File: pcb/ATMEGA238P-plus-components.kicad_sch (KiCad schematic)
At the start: 70 parts, among them J15 ICSP, J16 USB_B_Micro, J17 Conn_Coaxial, SW3 TS24CA_C393942, U3 ATMEGA328P-AU, U4 CH340G, U5 LM358DR, U6 74HC245, U7 nRF24L01P, U8 MICROSD_C164170, U9 74AHC1G125, Y3 16MHz, Y4 12MHz, Y5 16MHz

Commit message: pcb: switch SW1-SW3 to the TC-6610 THT tact switch (C7528713)
Replace the low-profile side-actuated TS24CA with a tall 9mm 6x6 THT
button that stays reachable on the assembled frame. The 4-pin part has
internally shorted pin pairs across its 6.5mm axis, so the distinct
1/2/3/4 pad numbering of the converted EasyEDA footprint would strap
each net across a shorted pair (STM32 held in reset); use KiCad's
official SW_PUSH_6mm_H9.5mm instead, whose paired 1,1,2,2 pads encode
the topology and drop onto the existing 2-pin symbols. Headless KiCad
10 ERC is identical before and after.
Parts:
- SW3: value TS24CA_C393942 -> TC-6610_C7528713; footprint easyeda:SW-SMD_2P-TS24CA -> Button_Switch_THT:SW_PUSH_6mm_H9.5mm; LCSC C393942 -> C7528713; Manufacturer SHOU HAN -> FG; Part TS24CA -> TC-6610 -6*6*9-260g
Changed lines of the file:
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@@
 			)
 		)
-		(property "Value" "TS24CA_C393942"
+		(property "Value" "TC-6610_C7528713"
 			(at 33.02 40.6399 90)
 			(hide yes)
@@
 			)
 		)
-		(property "Footprint" "easyeda:SW-SMD_2P-TS24CA"
+		(property "Footprint" "Button_Switch_THT:SW_PUSH_6mm_H9.5mm"
 			(at 34.29 39.37 0)
 			(hide yes)
@@
 			)
 		)
-		(property "Datasheet" "https://www.lcsc.com/datasheet/lcsc_datasheet_2404241539_SHOU-HAN-TS24CA_C393942.pdf"
+		(property "Datasheet" "https://wmsc.lcsc.com/wmsc/upload/file/pdf/v2/lcsc/2401191746_FG-TC-6610--6-6-9-260g_C7528713.pdf"
 			(at 34.29 39.37 0)
 			(hide yes)
@@
 			)
 		)
-		(property "Description" "Push button switch, generic, two pins"
+		(property "Description" "-20℃~+70℃ 12V 2.6N 50,000 cycles 50mA 6mm 6mm Black Round Button SPST Through Hole Without Bracket 插件-4P,6x6mm Tactile Switches ROHS"
 			(at 29.21 39.37 0)
 			(hide yes)
@@
 			)
 		)
-		(property "LCSC" "C393942"
+		(property "LCSC" "C7528713"
 			(at 29.21 39.37 0)
 			(hide yes)
@@
 			)
 		)
-		(property "Part" "TS24CA"
+		(property "Part" "TC-6610 -6*6*9-260g"
 			(at 29.21 39.37 0)
 			(hide yes)
@@
 			)
 		)
-		(property "Manufacturer" "SHOU HAN"
+		(property "Manufacturer" "FG"
 			(at 29.21 39.37 0)
 			(hide yes)

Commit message: pcb: 3D models for U3, U5, J3, J16
U3 and U5 move from the model-less DigiKey footprints to the official
KiCad TQFP-32 and SOIC-8 footprints, whose STEP models ship with the
AppImage. J3/J16's micro-USB footprint had no model, no MPN, and
unknown provenance - replaced wholesale with the SHOU HAN MicroXNJ
(C404969): converted footprint with shell legs renumbered to the
Shield pin 6, STEP model, and BOM fields, verified against its
datasheet drawing. ERC caught that the LM358 is multi-unit and the
first edit only touched U5A's footprint field; U5B fixed to match.
Headless KiCad 10 ERC identical to baseline.
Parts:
- J16: footprint easyeda:MICRO-USB-SMD_5P-P0.65-H-F_MICRO5.9MMUSB -> easyeda:MICRO-USB-SMD_MICROXNJ_1; LCSC (none) -> C404969; Manufacturer (none) -> SHOU HAN; Part (none) -> MicroXNJ
- U3: footprint digikey-footprints:TQFP-32_7x7mm -> Package_QFP:TQFP-32_7x7mm_P0.8mm
- U5: footprint digikey-footprints:SOIC-8_W3.9mm -> Package_SO:SOIC-8_3.9x4.9mm_P1.27mm
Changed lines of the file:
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@@
 			)
 		)
-		(property "Footprint" "digikey-footprints:SOIC-8_W3.9mm"
+		(property "Footprint" "Package_SO:SOIC-8_3.9x4.9mm_P1.27mm"
 			(at 41.91 203.2 0)
 			(hide yes)
@@
 			)
 		)
-		(property "Footprint" "easyeda:MICRO-USB-SMD_5P-P0.65-H-F_MICRO5.9MMUSB"
+		(property "Footprint" "easyeda:MICRO-USB-SMD_MICROXNJ_1"
 			(at 43.18 247.65 0)
 			(hide yes)
@@
 			)
 		)
-		(property "Datasheet" ""
+		(property "Datasheet" "https://www.lcsc.com/datasheet/lcsc_datasheet_2204151400_SHOU-HAN-MicroXNJ_C404969.pdf"
 			(at 43.18 247.65 0)
 			(hide yes)
@@
 			)
 		)
-		(property "Description" "USB Micro Type B connector"
+		(property "Description" "-20℃~+85℃ 1 1.8A 30V 5,000 times 5P Black Female Micro-B Surface Mount, Right Angle USB 2.0 SMD USB Connectors ROHS"
 			(at 39.37 246.38 0)
 			(hide yes)
@@
 			)
 		)
+    (property "LCSC" "C404969" (at 39.37 246.38 0)
+      (effects (font (size 1.27 1.27)) (hide yes))
+    )
+    (property "Part" "MicroXNJ" (at 39.37 246.38 0)
+      (effects (font (size 1.27 1.27)) (hide yes))
+    )
+    (property "Manufacturer" "SHOU HAN" (at 39.37 246.38 0)
+      (effects (font (size 1.27 1.27)) (hide yes))
+    )
 		(pin "3"
 		)
@@
 			)
 		)
-		(property "Footprint" "digikey-footprints:TQFP-32_7x7mm"
+		(property "Footprint" "Package_QFP:TQFP-32_7x7mm_P0.8mm"
 			(at 171.45 87.63 0)
 			(hide yes)
@@
 			)
 		)
-		(property "Footprint" "digikey-footprints:SOIC-8_W3.9mm"
+		(property "Footprint" "Package_SO:SOIC-8_3.9x4.9mm_P1.27mm"
 			(at 41.91 180.34 0)
 			(hide yes)

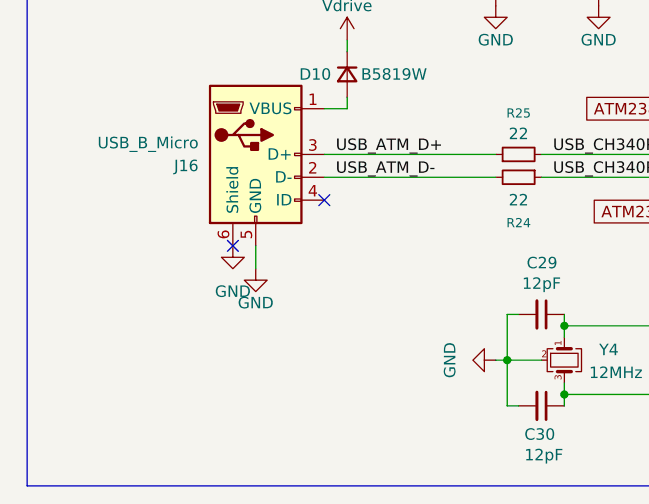
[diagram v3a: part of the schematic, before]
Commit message: pcb: import the new U3/U5/USB footprints onto the board
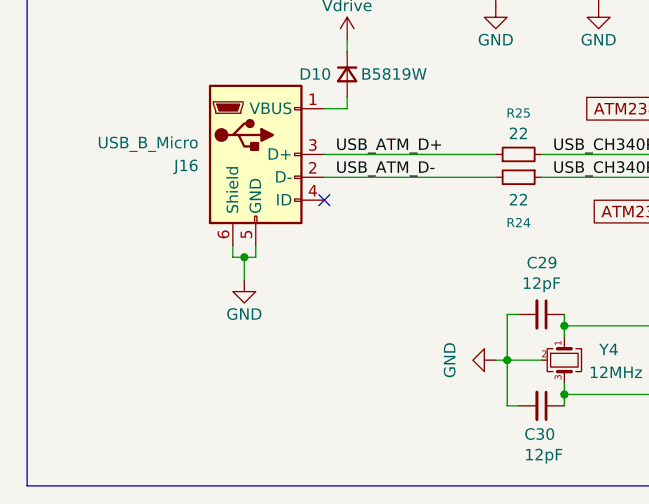
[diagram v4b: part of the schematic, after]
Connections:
- no-connect marks 20 -> 19
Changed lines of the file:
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@@
 	)
 	(junction
+		(at 38.1 257.81)
+		(diameter 0)
+		(color 0 0 0 0)
+	)
+	(junction
 		(at 177.8 256.54)
 		(diameter 0)
@@
 	)
 	(no_connect
-		(at 36.83 256.54)
-	)
-	(no_connect
 		(at 153.67 80.01)
 	)
@@
 	(wire
 		(pts
-			(xy 39.37 256.54) (xy 39.37 259.08)
+			(xy 38.1 257.81) (xy 38.1 260.35)
 		)
 		(stroke
@@
 	(wire
 		(pts
+			(xy 39.37 257.81) (xy 39.37 256.54)
+		)
+		(stroke
+			(width 0)
+			(type default)
+		)
+	)
+	(wire
+		(pts
 			(xy 118.11 238.76) (xy 115.57 238.76)
 		)
@@
 	(wire
 		(pts
+			(xy 38.1 257.81) (xy 39.37 257.81)
+		)
+		(stroke
+			(width 0)
+			(type default)
+		)
+	)
+	(wire
+		(pts
 			(xy 91.44 254) (xy 91.44 265.43)
 		)
@@
 	(wire
 		(pts
+			(xy 36.83 257.81) (xy 38.1 257.81)
+		)
+		(stroke
+			(width 0)
+			(type default)
+		)
+	)
+	(wire
+		(pts
 			(xy 274.32 241.3) (xy 274.32 243.84)
 		)
@@
 	(wire
 		(pts
+			(xy 36.83 256.54) (xy 36.83 257.81)
+		)
+		(stroke
+			(width 0)
+			(type default)
+		)
+	)
+	(wire
+		(pts
 			(xy 173.99 27.94) (xy 173.99 22.86)
 		)
@@
 	(symbol
 		(lib_id "PCM_SparkFun-PowerSymbol:GND")
-		(at 39.37 259.08 0)
+		(at 38.1 260.35 0)
 		(unit 1)
 		(body_style 1)
@@
 		(fields_autoplaced yes)
 		(property "Reference" "#PWR079"
-			(at 39.37 265.43 0)
+			(at 38.1 266.7 0)
 			(hide yes)
 			(show_name no)
@@
 		)
 		(property "Value" "GND"
-			(at 39.37 262.89 0)
+			(at 38.1 264.16 0)
 			(show_name no)
 			(do_not_autoplace yes)
@@
 		)
 		(property "Footprint" ""
-			(at 39.37 259.08 0)
+			(at 38.1 260.35 0)
 			(hide yes)
 			(show_name no)
@@
 		)
 		(property "Datasheet" ""
-			(at 39.37 259.08 0)
+			(at 38.1 260.35 0)
 			(hide yes)
 			(show_name no)
@@
 		)
 		(property "Description" "Power symbol creates a global label with name \"GND\" , ground"
-			(at 39.37 267.97 0)
+			(at 38.1 269.24 0)
 			(hide yes)
 			(show_name no)
@@
 			)
 		)
-    (property "LCSC" "C404969" (at 39.37 246.38 0)
-      (effects (font (size 1.27 1.27)) (hide yes))
-    )
-    (property "Part" "MicroXNJ" (at 39.37 246.38 0)
-      (effects (font (size 1.27 1.27)) (hide yes))
-    )
-    (property "Manufacturer" "SHOU HAN" (at 39.37 246.38 0)
-      (effects (font (size 1.27 1.27)) (hide yes))
-    )
+		(property "LCSC" "C404969"
+			(at 39.37 246.38 0)
+			(hide yes)
+			(show_name no)
+			(do_not_autoplace no)
+			(effects
+				(font
+					(size 1.27 1.27)
+				)
+			)
+		)
+		(property "Part" "MicroXNJ"
+			(at 39.37 246.38 0)
+			(hide yes)
+			(show_name no)
+			(do_not_autoplace no)
+			(effects
+				(font
+					(size 1.27 1.27)
+				)
+			)
+		)
+		(property "Manufacturer" "SHOU HAN"
+			(at 39.37 246.38 0)
+			(hide yes)
+			(show_name no)
+			(do_not_autoplace no)
+			(effects
+				(font
+					(size 1.27 1.27)
+				)
+			)
+		)
 		(pin "3"
 		)
@@
 					(unit 1)
 				)
-			)
-		)
-	)
-	(symbol
-		(lib_id "power:GND")
-		(at 36.83 256.54 0)
-		(unit 1)
-		(body_style 1)
-		(exclude_from_sim no)
-		(in_bom yes)
-		(on_board yes)
-		(in_pos_files yes)
-		(dnp no)
-		(fields_autoplaced yes)
-		(property "Reference" "#PWR0143"
-			(at 36.83 262.89 0)
-			(hide yes)
-			(show_name no)
-			(do_not_autoplace no)
-			(effects
-				(font
-					(size 1.27 1.27)
-				)
-			)
-		)
-		(property "Value" "GND"
-			(at 36.83 261.62 0)
-			(show_name no)
-			(do_not_autoplace no)
-			(effects
-				(font
-					(size 1.27 1.27)
-				)
-			)
-		)
-		(property "Footprint" ""
-			(at 36.83 256.54 0)
-			(hide yes)
-			(show_name no)
-			(do_not_autoplace no)
-			(effects
-				(font
-					(size 1.27 1.27)
-				)
-			)
-		)
-		(property "Datasheet" ""
-			(at 36.83 256.54 0)
-			(hide yes)
-			(show_name no)
-			(do_not_autoplace no)
-			(effects
-				(font
-					(size 1.27 1.27)
-				)
-			)
-		)
-		(property "Description" "Power symbol creates a global label with name GND, ground"
-			(at 36.83 256.54 0)
-			(hide yes)
-			(show_name no)
-			(do_not_autoplace no)
-			(effects
-				(font
-					(size 1.27 1.27)
-				)
-			)
-		)
-		(pin "1"
-		)
-		(instances
-			(project "drone-flight-controller"
-				(path "/2753c1d5-c5b3-42f6-8923-cca974813b6b/3ba11137-7aba-429f-b0d2-26d56a1546d6"
-					(reference "#PWR0143")
-					(unit 1)
-				)

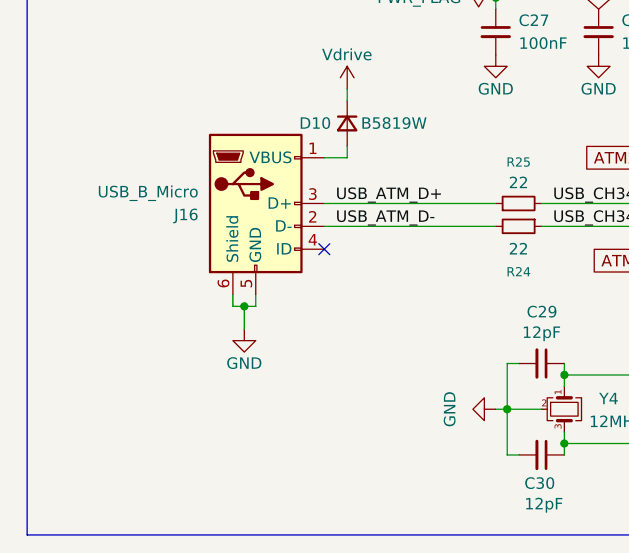
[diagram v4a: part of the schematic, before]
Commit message: pcb: session state - U10 folded on board, pending sch fixes
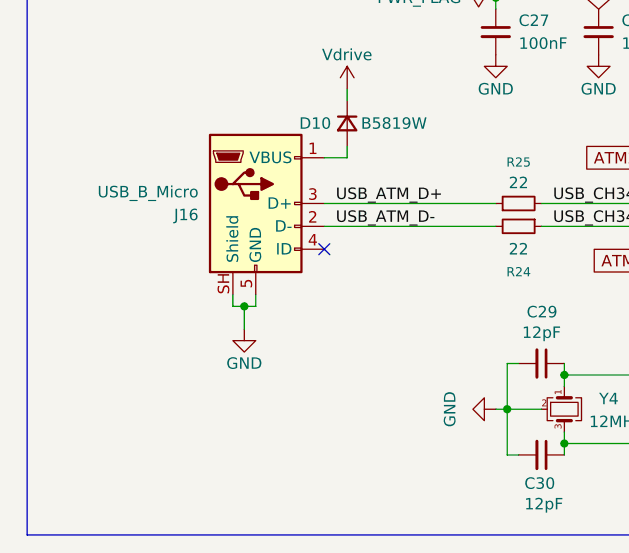
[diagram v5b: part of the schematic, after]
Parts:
- U3: footprint Package_QFP:TQFP-32_7x7mm_P0.8mm -> digikey-footprints:TQFP-32_7x7mm
- U5: footprint Package_SO:SOIC-8_3.9x4.9mm_P1.27mm -> digikey-footprints:SOIC-8_W3.9mm
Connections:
- net GND: now also J16.SH (Shield); no longer J16.6 (Shield)
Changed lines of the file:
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@@
 			)
 		)
-		(property "Footprint" "Package_SO:SOIC-8_3.9x4.9mm_P1.27mm"
+		(property "Footprint" "digikey-footprints:SOIC-8_W3.9mm"
 			(at 41.91 203.2 0)
 			(hide yes)
@@
 			)
 		)
-		(property "Description" "-20℃~+85℃ 1 1.8A 30V 5,000 times 5P Black Female Micro-B Surface Mount, Right Angle USB 2.0 SMD USB Connectors ROHS"
+		(property "Description" "USB Micro Type B connector"
 			(at 39.37 246.38 0)
 			(hide yes)
@@
 		(pin "1"
 		)
-		(pin "6"
+		(pin "SH"
 		)
 		(pin "4"
@@
 			)
 		)
-		(property "Description" "-20℃~+70℃ 12V 2.6N 50,000 cycles 50mA 6mm 6mm Black Round Button SPST Through Hole Without Bracket 插件-4P,6x6mm Tactile Switches ROHS"
+		(property "Description" "Push button switch, generic, two pins"
 			(at 29.21 39.37 0)
 			(hide yes)
@@
 			)
 		)
-		(property "Footprint" "Package_QFP:TQFP-32_7x7mm_P0.8mm"
+		(property "Footprint" "digikey-footprints:TQFP-32_7x7mm"
 			(at 171.45 87.63 0)
 			(hide yes)
@@
 			)
 		)
-		(property "Footprint" "Package_SO:SOIC-8_3.9x4.9mm_P1.27mm"
+		(property "Footprint" "digikey-footprints:SOIC-8_W3.9mm"
 			(at 41.91 180.34 0)
 			(hide yes)

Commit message: pcb: re-apply U3/U5 footprints durably; fix U10 sch/board mismatch and U2 3D path
A symbol-update-with-reset-fields pass reverted U3 and U5 to the
model-less DigiKey footprints because the embedded library defaults
still carried them - re-apply the official footprints on the instances
AND the embedded lib_symbol defaults so a future reset cannot regress
them again. Align U10's schematic with the board's folded
TO-220-3_Horizontal_TabDown (the schematic still said the 4-lead
variant, which a footprint-replacing import would have restored). Point
U2's model at the QFN-24 EP2.6x2.6 step that actually ships - the
Sensor_Motion footprint references an EP2.7x2.6 file that does not
exist in the 3D lib. ERC otherwise identical; two new intentional
lib_symbol_mismatch warnings record that the embedded ATmega/LM7805
defaults now deliberately diverge from the external libraries.
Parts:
- U3: footprint digikey-footprints:TQFP-32_7x7mm -> Package_QFP:TQFP-32_7x7mm_P0.8mm
- U5: footprint digikey-footprints:SOIC-8_W3.9mm -> Package_SO:SOIC-8_3.9x4.9mm_P1.27mm
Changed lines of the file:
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@@
 			)
 		)
-		(property "Footprint" "digikey-footprints:SOIC-8_W3.9mm"
+		(property "Footprint" "Package_SO:SOIC-8_3.9x4.9mm_P1.27mm"
 			(at 41.91 203.2 0)
 			(hide yes)
@@
 			)
 		)
-		(property "Footprint" "digikey-footprints:TQFP-32_7x7mm"
+		(property "Footprint" "Package_QFP:TQFP-32_7x7mm_P0.8mm"
 			(at 171.45 87.63 0)
 			(hide yes)
@@
 			)
 		)
-		(property "Footprint" "digikey-footprints:SOIC-8_W3.9mm"
+		(property "Footprint" "Package_SO:SOIC-8_3.9x4.9mm_P1.27mm"
 			(at 41.91 180.34 0)
 			(hide yes)

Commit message: pcb: source the entire remaining BOM against the LCSC catalog
Jellybean MPN sweep: ~142 refs across 61 groups - every IC, passive,
LED, diode, crystal, RF inductor, ferrite, and connector now carries
LCSC/Part/Manufacturer/Datasheet fields, resolved offline Basic-first.
Crystals were matched on load capacitance to the repo's original
datasheets, the polarized 10uF pair is the exact original tantalum,
and the nRF matching network gets proper RF multilayer parts. Two
physical deltas: Y2's footprint grows 2012 -> 3215 to fit the Basic
Epson FC-135, and FB1/FB2's invalid "100Uhm" value becomes the
sourced 3A 120R power bead. Sourcing gate: PASS, 0 blocking, 26
Extended lines (~$78 max setup). ERC identical.
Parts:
- C20, C21, C22, C24, C27, C28, C31, C32, C33, C45, C47: LCSC (none) -> C1525; Manufacturer (none) -> Samsung Electro-Mechanics; Part (none) -> CL05B104KO5NNNC
- C23, C46: LCSC (none) -> C307423; Manufacturer (none) -> Samsung Electro-Mechanics; Part (none) -> CL05A475MQ5NRNC
- C25, C26, C29, C30, C43, C44: LCSC (none) -> C1547; Manufacturer (none) -> FH(Guangdong Fenghua Advanced Tech); Part (none) -> 0402CG120J500NT
- C34, C35, C36: LCSC (none) -> C15195; Manufacturer (none) -> Samsung Electro-Mechanics; Part (none) -> CL05B103KB5NNNC
- C37: LCSC (none) -> C52923; Manufacturer (none) -> Samsung Electro-Mechanics; Part (none) -> CL05A105KA5NQNC
- C38: LCSC (none) -> C106862; Manufacturer (none) -> YAGEO; Part (none) -> CC0402KRX7R9BB333
- C39: LCSC (none) -> C1552; Manufacturer (none) -> FH(Guangdong Fenghua Advanced Tech); Part (none) -> 0402CG1R5C500NT
- C40: LCSC (none) -> C1550; Manufacturer (none) -> FH(Guangdong Fenghua Advanced Tech); Part (none) -> 0402CG1R0C500NT
- C41: LCSC (none) -> C1531; Manufacturer (none) -> FH(Guangdong Fenghua Advanced Tech); Part (none) -> 0402B222K500NT
- C42: LCSC (none) -> C1538; Manufacturer (none) -> FH(Guangdong Fenghua Advanced Tech); Part (none) -> 0402B472K500NT
- D10: LCSC (none) -> C64885; Manufacturer (none) -> MDD（Microdiode Electronics）; Part (none) -> B5819W
- D11, D12, D18: LCSC (none) -> C12624; Manufacturer (none) -> Hubei KENTO Elec; Part (none) -> KT-0603G
- D13, D15: LCSC (none) -> C2286; Manufacturer (none) -> Hubei KENTO Elec; Part (none) -> KT-0603R
- D16: LCSC (none) -> C2288; Manufacturer (none) -> Hubei KENTO Elec; Part (none) -> KT-0603B
- J15: LCSC (none) -> C492420; Manufacturer (none) -> XFCN; Part (none) -> PZ254V-12-6P
- J17: LCSC (none) -> C496551; Manufacturer (none) -> BAT WIRELESS; Part (none) -> BWSMA-KWE-Z001
- L2: LCSC (none) -> C98003; Manufacturer (none) -> Murata Electronics; Part (none) -> LQG15HS8N2J02D
- L3: LCSC (none) -> C14033; Manufacturer (none) -> Sunlord; Part (none) -> SDCL1005C3N9STDF
- L4: LCSC (none) -> C27123; Manufacturer (none) -> Sunlord; Part (none) -> SDCL1005C2N7STDF
- R21, R30, R33, R35, R36: LCSC (none) -> C25744; Manufacturer (none) -> UNI-ROYAL(Uniroyal Elec); Part (none) -> 0402WGF1002TCE
- R22: LCSC (none) -> C25104; Manufacturer (none) -> UNI-ROYAL(Uniroyal Elec); Part (none) -> 0402WGF3300TCE
- R23, R28, R32: LCSC (none) -> C21190; Manufacturer (none) -> UNI-ROYAL(Uniroyal Elec); Part (none) -> 0603WAF1001T5E
- R24, R25: LCSC (none) -> C25092; Manufacturer (none) -> UNI-ROYAL(Uniroyal Elec); Part (none) -> 0402WGF220JTCE
- R26, R27: LCSC (none) -> C11702; Manufacturer (none) -> UNI-ROYAL(Uniroyal Elec); Part (none) -> 0402WGF1001TCE
- R29, R31: LCSC (none) -> C22843; Manufacturer (none) -> UNI-ROYAL(Uniroyal Elec); Part (none) -> 0603WAF1501T5E
- R34: LCSC (none) -> C23179; Manufacturer (none) -> UNI-ROYAL(Uniroyal Elec); Part (none) -> 0603WAF4700T5E
- R37: LCSC (none) -> C26083; Manufacturer (none) -> UNI-ROYAL(Uniroyal Elec); Part (none) -> 0402WGF1004TCE
- R38: LCSC (none) -> C25900; Manufacturer (none) -> UNI-ROYAL(Uniroyal Elec); Part (none) -> 0402WGF4701TCE
- U3: LCSC (none) -> C14877; Manufacturer Microchip Technology -> Microchip Tech; Part (none) -> ATMEGA328P-AU
- U4: LCSC (none) -> C14267; Manufacturer (none) -> WCH(Jiangsu Qin Heng); Part (none) -> CH340G
- U5: LCSC (none) -> C5423; Part (none) -> LM358DR
- U6: LCSC (none) -> C10093; Manufacturer (none) -> Texas Instruments; Part (none) -> SN74HC245DWR
- U7: LCSC (none) -> C8791; Manufacturer (none) -> Nordic Semicon; Part (none) -> NRF24L01P-R
- U8: LCSC (none) -> C164170; Manufacturer (none) -> MOLEX; Part (none) -> 472192001
- U9: LCSC (none) -> C151890; Manufacturer (none) -> Texas Instruments; Part (none) -> SN74AHC1G125DCKR
- Y3, Y5: LCSC (none) -> C13738; Manufacturer (none) -> Yangxing Tech; Part (none) -> X322516MLB4SI
- Y4: LCSC (none) -> C9002; Manufacturer (none) -> Yangxing Tech; Part (none) -> X322512MSB4SI

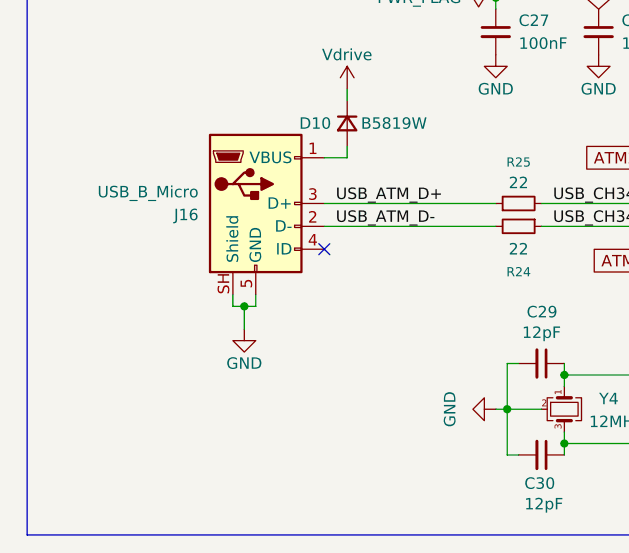
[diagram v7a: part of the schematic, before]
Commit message: sch: make the USB shield fix immune to symbol updates
'Update Symbols from Library' restored the global Connector lib's stale
SH shield pin for the second time, floating both USB shells again.
Re-apply SH->6 and make it structural: the corrected USB_B_Micro now
lives in the project's custom-symbols library, sym-lib-table registers
it (previously empty), and J3/J16 resolve project-locally - a future
symbol update pulls the corrected copy by construction. Netlist
verified: both shield pins back on GND.
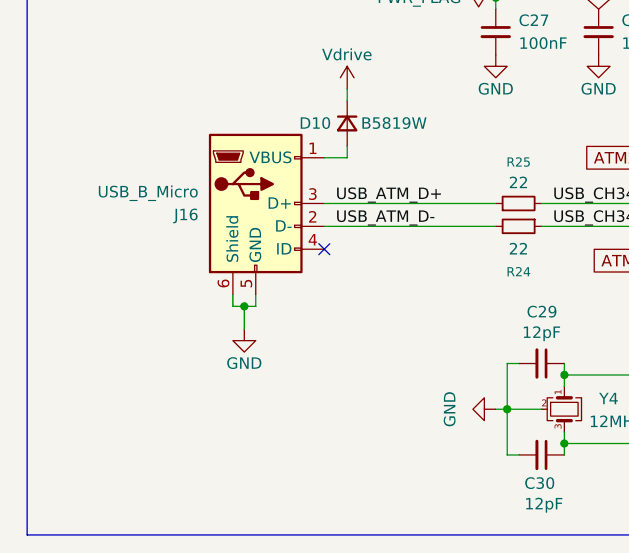
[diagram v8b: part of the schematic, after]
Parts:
- J16: symbol Connector:USB_B_Micro -> custom-symbols:USB_B_Micro
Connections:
- net GND: now also J16.6 (Shield); no longer J16.SH (Shield)
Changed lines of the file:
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@@
 	)
 	(symbol
-		(lib_id "Connector:USB_B_Micro")
+		(lib_id "custom-symbols:USB_B_Micro")
 		(at 39.37 246.38 0)
 		(unit 1)
@@
 		(pin "1"
 		)
-		(pin "SH"
+		(pin "6"
 		)
 		(pin "4"
